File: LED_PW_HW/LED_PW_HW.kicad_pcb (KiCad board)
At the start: 4 copper layers, 44 x 44 mm, 164 parts, among them SW1 SW_MEC_5E, U2 STM32L031K6Tx, Y1 Crystal

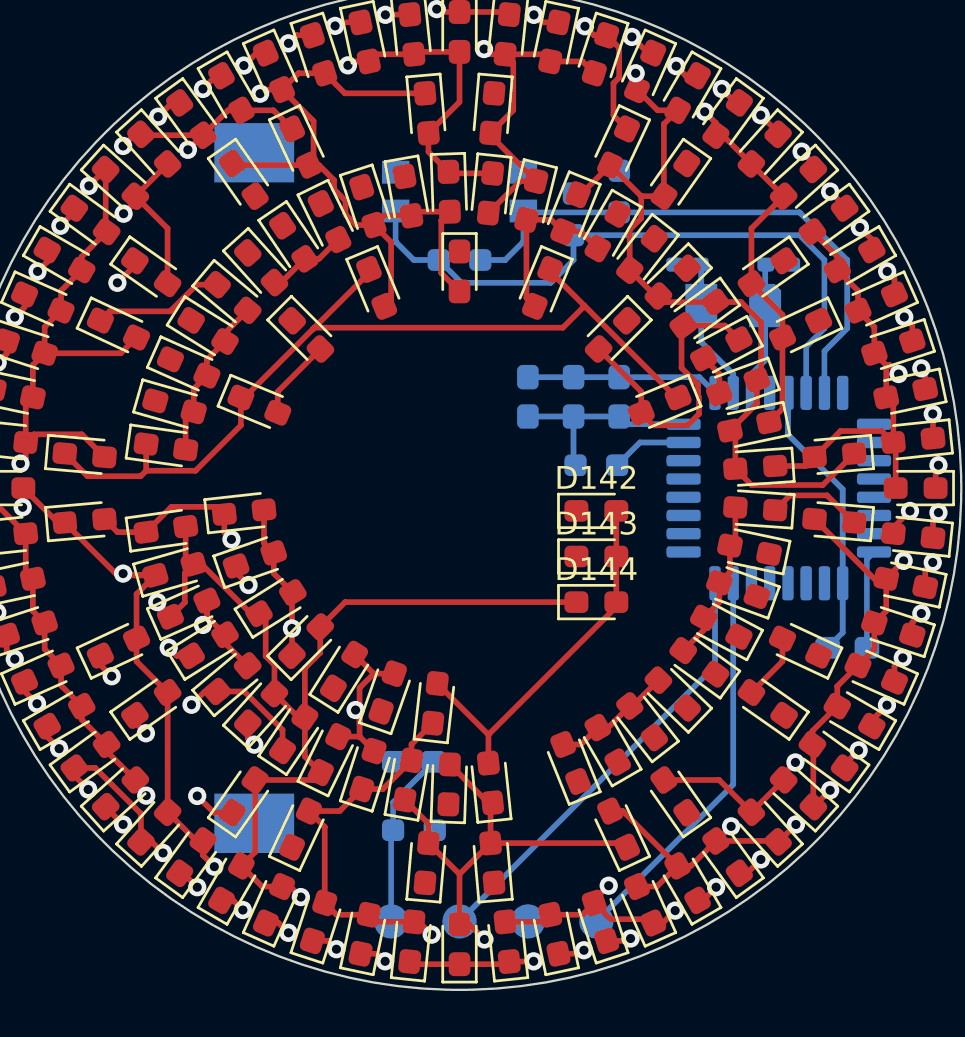
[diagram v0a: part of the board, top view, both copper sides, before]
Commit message: v3 is a cleaner v1
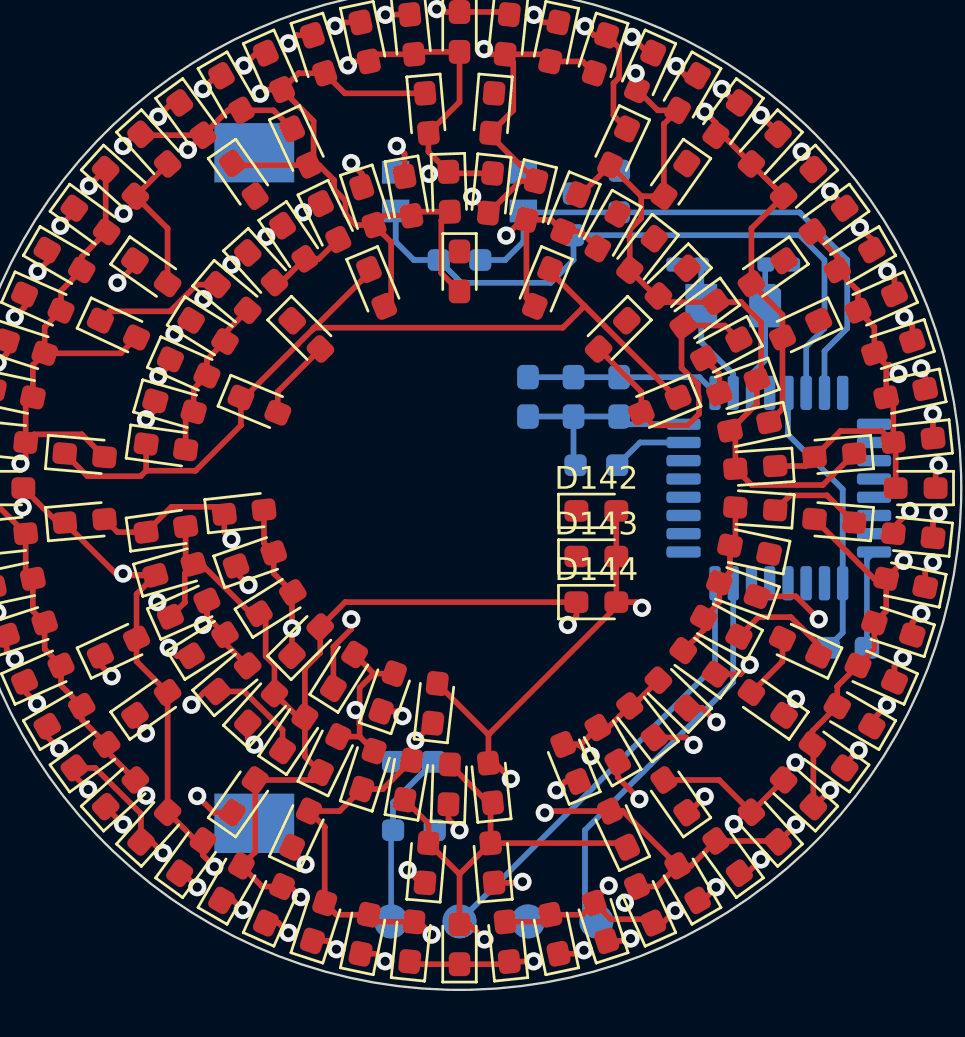
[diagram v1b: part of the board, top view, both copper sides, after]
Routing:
- net CB6: track 39.8 -> 85.5 mm, vias 4 -> 10
- net CB7: track 33.6 -> 78.8 mm, vias 8 -> 11
- net CB4: track 40.1 -> 60.8 mm, vias 4 -> 6
- net CA6: track 30.4 -> 47.8 mm, vias 3 -> 7
- net CB8: track 30.7 -> 47.0 mm, vias 8 -> 10
- net CB2: track 39.8 -> 51.9 mm, vias 6 -> 8
- net CB1: track 40.7 -> 52.2 mm, vias 3 -> 5
- net CA7: track 36.3 -> 47.7 mm, vias 2 -> 5
- net CB9: track 30.5 -> 40.8 mm
- net CA5: track 27.6 -> 36.8 mm, vias 2 -> 6
- net CA8: track 22.0 -> 31.0 mm, vias 4 -> 5
- net CB3: track 54.0 -> 60.3 mm, vias 4 -> 7
- net CB5: track 50.4 -> 52.1 mm, vias 6 -> 7
